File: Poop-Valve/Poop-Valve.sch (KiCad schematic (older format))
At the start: 45 parts, among them J1 RaspberryPi, J10 Valve Sig, J11 Conn_01x02_Male, J12 Relays, J13 LEDs, J14 24VDC, J15 Sensor, J16 Grove LCD, J2 Valve, J3 Charger, J4 Override, J5 Ovr Switch, J6 Power, J7 12VDC, J8 Conn_01x02_Male, J9 Conn_01x02_Male, K1 Override Relays, K2 Polarity Reverse, K3 Enable Relays, K4 Relay_Module, K5 Direction Relays, K6 Polarity Reverse, SW1 Override, SW2 SW_DPDT_x2, SW3 Open/Close, U1 Opened, U2 Closed, U3 Override, U4 MCP3008

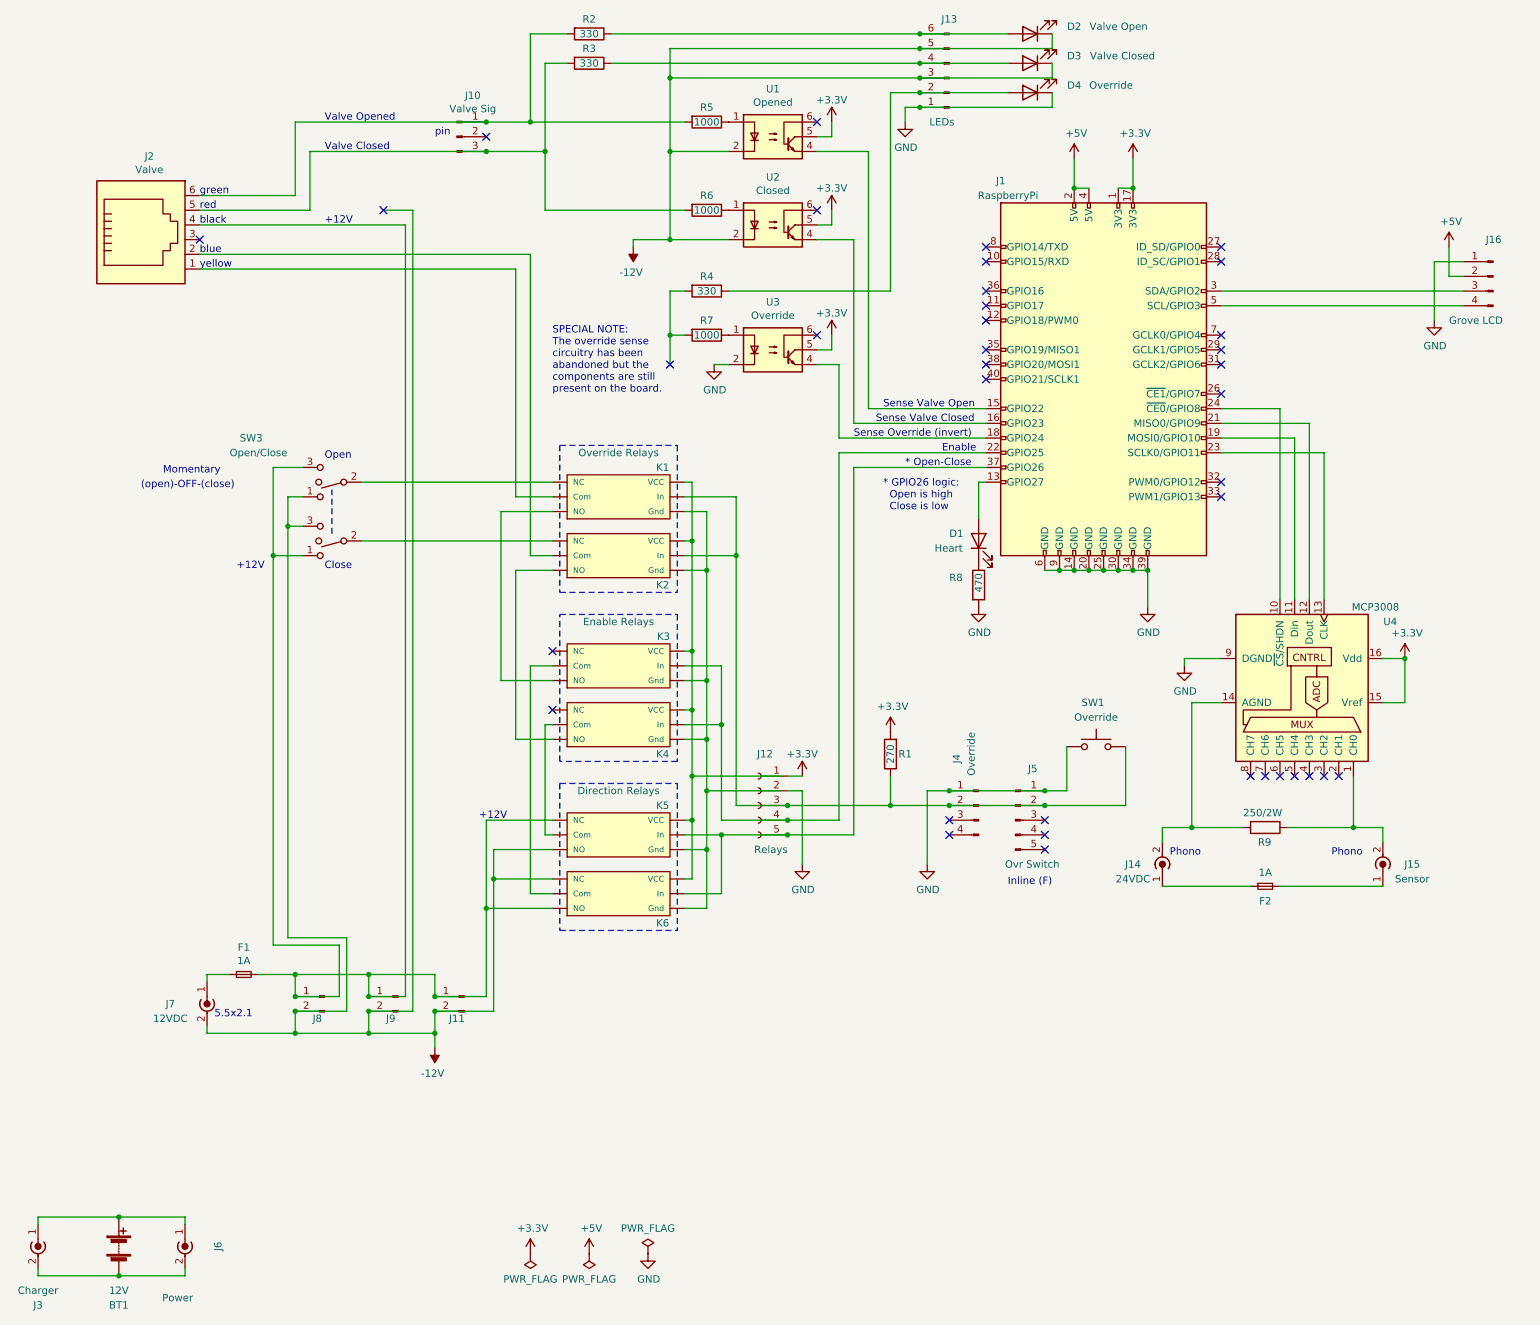
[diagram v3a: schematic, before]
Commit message: v0.9 add override shunt and sense transistors
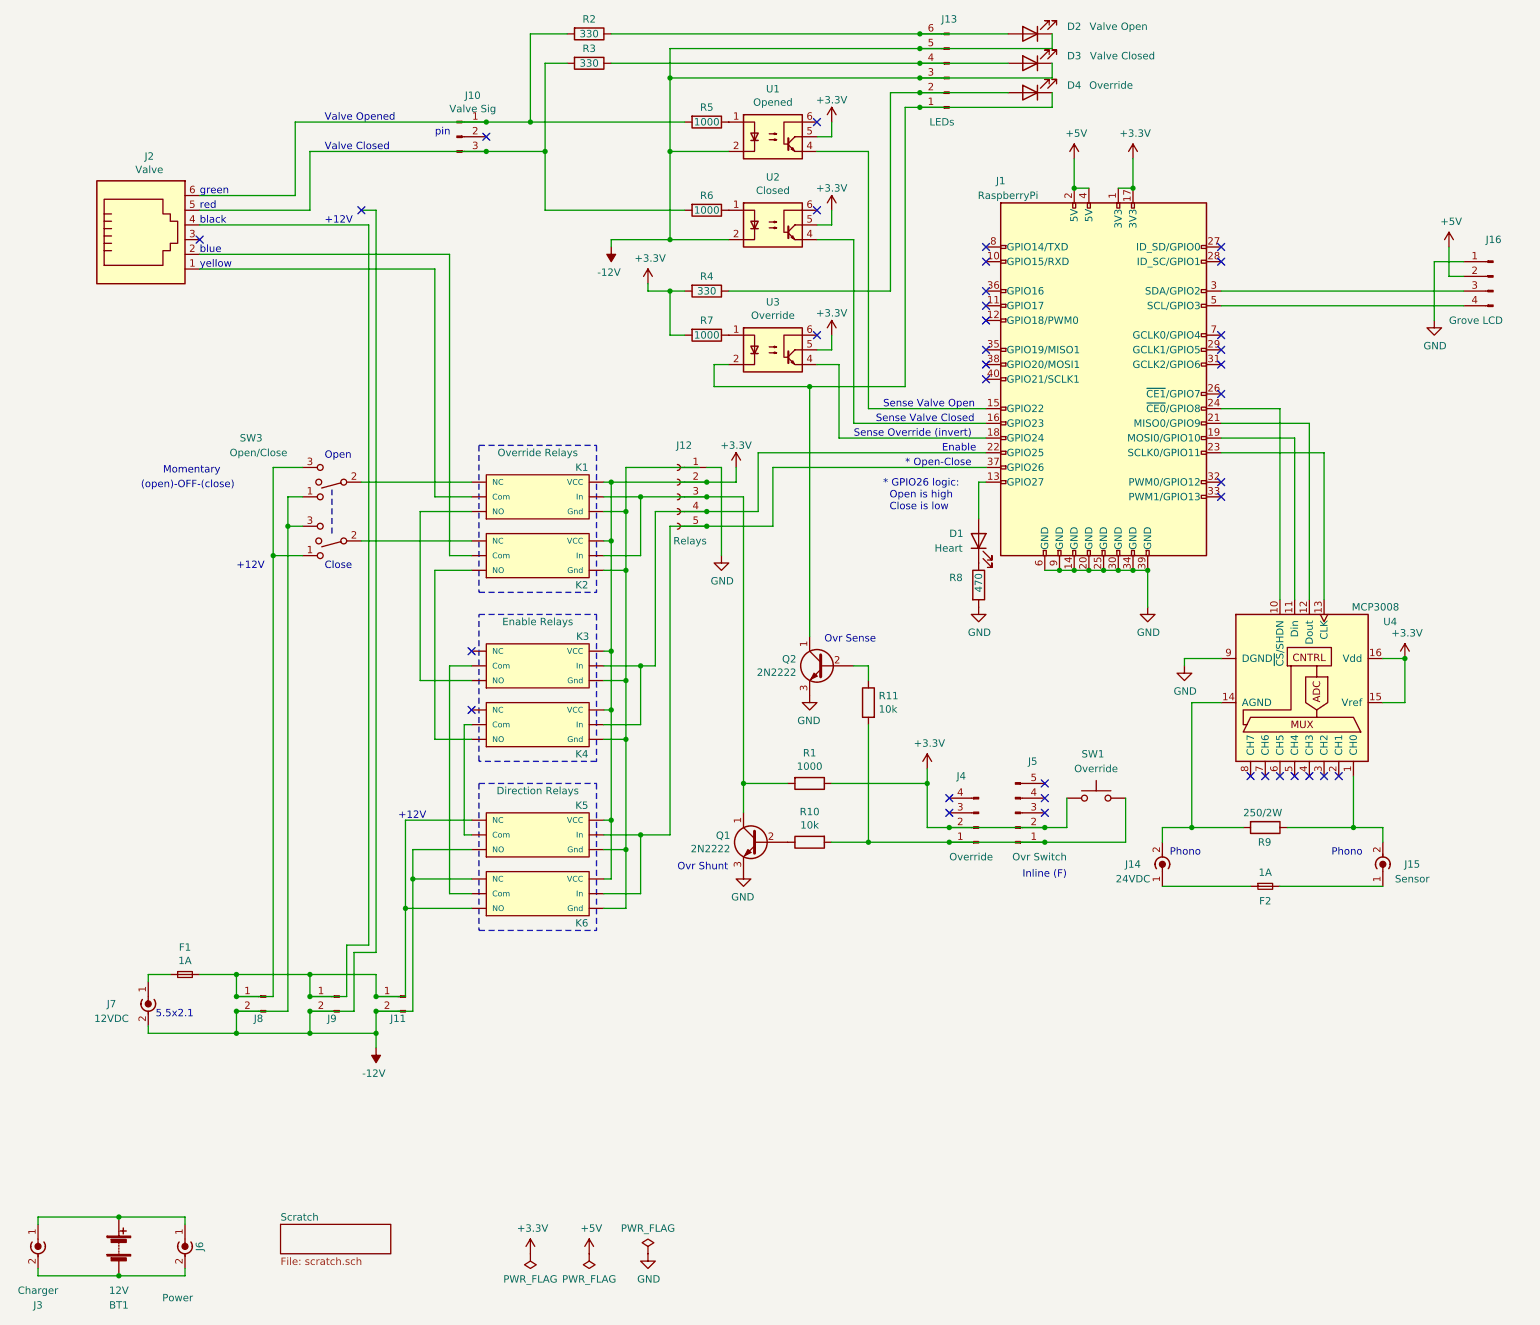
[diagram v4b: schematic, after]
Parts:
- added Q1, Q2: 2N2222, symbol Device:Q_NPN_CBE
- added R10, R11: 10k, symbol Device:R
- R1: value 270 -> 1000
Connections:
- net +3V3: now also J12.2 (Pin_2), J4.2 (Pin_2), J5.2 (Pin_2), K1.~ (VCC), K2.~ (VCC), K3.~ (VCC), K4.~ (VCC), K5.~ (VCC), K6.~ (VCC), R1.1, R4.2, R7.2, SW1.2; no longer J12.1 (Pin_1), R1.2
- net GND: now also J12.1 (Pin_1), Q1.3 (E), Q2.3 (E); no longer D4.1 (K), J12.2 (Pin_2), J13.1 (Pin_1), J4.1 (Pin_1), J5.1 (Pin_1), SW1.2, U3.2
- new net: K1.~ (VCC), K2.~ (VCC), K3.~ (VCC), K4.~ (VCC), K5.~ (VCC), K6.~ (VCC)
- new net: K1.~ (VCC), K3.~ (VCC)
- new net: K3.~ (VCC), K6.~ (VCC)
- new net: K2.~ (VCC), K4.~ (VCC)
- new net: K4.~ (VCC), K5.~ (VCC)
- new net: D4.1 (K), J13.1 (Pin_1), Q2.1 (C), U3.2
- new net: J4.1 (Pin_1), J5.1 (Pin_1), R10.2, R11.2, SW1.1
- new net: J12.3 (Pin_3), K1.~ (VCC), K2.~ (VCC), Q1.1 (C), R1.2
- new net: Q1.2 (B), R10.1
- new net: Q2.2 (B), R11.1
- no-connect marks 37 -> 36
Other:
- note added: "Ovr Sense"
- note added: "Ovr Shunt"
- note removed: "SPECIAL NOTE:\nThe override sense\ncircuitry has been\nabandoned but the\ncomponents are still\npresent on the board."
- moved on the sheet: F1, J11, J12, J4, J5, J7, J8, J9, K1, K2, K3, K4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

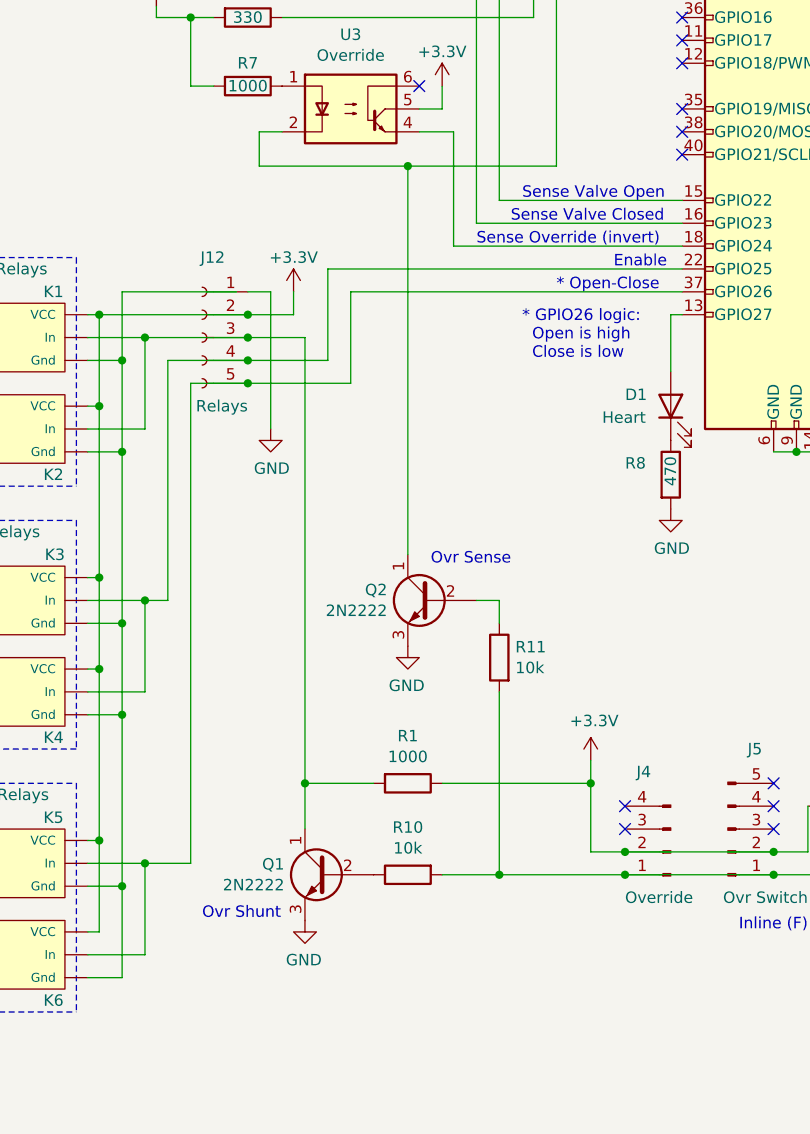
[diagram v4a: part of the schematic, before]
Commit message: v0.10 add Master Override switch
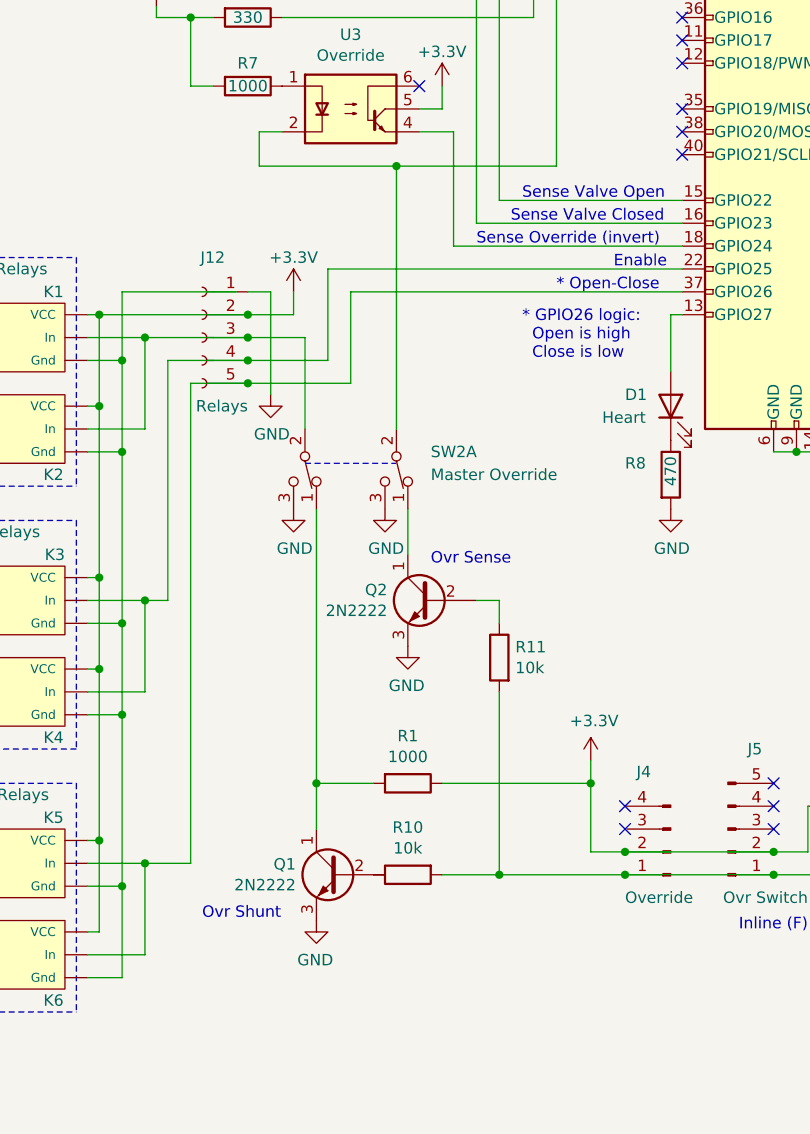
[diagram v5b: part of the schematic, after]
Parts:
- added SW2: Master Override, symbol Switch:SW_SPDT_SMALL
- added SW?: SW_SPDT_SMALL, symbol Switch:SW_SPDT_SMALL
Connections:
- net GND: now also SW2.3 (C), SW?.3 (C)
- net at D4.1 (K), J13.1 (Pin_1), U3.2: now also SW2.2 (B); no longer Q2.1 (C)
- net at Q1.2 (B): no longer R10.1
- new net: K1.~ (VCC), K2.~ (VCC), K3.~ (VCC), K4.~ (VCC), K5.~ (VCC), K6.~ (VCC)
- new net: K1.~ (VCC), K3.~ (VCC)
- new net: K3.~ (VCC), K6.~ (VCC)
- new net: K2.~ (VCC), K4.~ (VCC)
- new net: K4.~ (VCC), K5.~ (VCC)
- new net: J12.3 (Pin_3), K1.~ (VCC), K2.~ (VCC), SW?.2 (B)
- new net: Q1.1 (C), R1.2, SW?.1 (A)
- new net: Q2.1 (C), SW2.1 (A)
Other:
- moved on the sheet: Q1
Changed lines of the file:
@@
 Sheet 1 2
 Title "Poop Valve Controller"
-Date "2023-01-29"
-Rev "0.9 (draft)"
+Date "2023-02-01"
+Rev "0.10 (draft)"
 Comp "Robert Ferguson Observatory"
-Comment1 "v0.6 fix led connector pinout"
-Comment2 "v0.7 correct ADC sample wiring"
-Comment3 "v0.8 reconfigure manual override; updated layout for clarity"
-Comment4 "v0.9 add override shunt and sense transistors "
+Comment1 "v0.7 correct ADC sample wiring"
+Comment2 "v0.8 reconfigure manual override; updated layout for clarity"
+Comment3 "v0.9 add override shunt and sense transistors "
+Comment4 "v0.10 add Master Override switch"
 $EndDescr
 $Comp
@@
 Wire Wire Line
 	4700 2500 4800 2500
-$Comp
-L power:GND #PWR012
-U 1 1 65D19661
-P 5050 4300
-F 0 "#PWR012" H 5050 4050 50  0001 C CNN
-F 1 "GND" H 5055 4127 50  0000 C CNN
-F 2 "" H 5050 4300 50  0001 C CNN
-F 3 "" H 5050 4300 50  0001 C CNN
-	1    5050 4300
-	1    0    0    -1
-$EndComp
 Wire Wire Line
 	4950 3900 5200 3900
@@
 L Device:Q_NPN_CBE Q?
 U 1 1 6627A4F5
-P 5300 6250
+P 5350 6250
 AR Path="/65DFE627/6627A4F5" Ref="Q?"  Part="1"
 AR Path="/6627A4F5" Ref="Q1"  Part="1"
-F 0 "Q1" H 5490 6296 50  0000 L CNN
-F 1 "2N2222" H 5490 6205 50  0000 L CNN
-F 2 "" H 5500 6350 50  0001 C CNN
-F 3 "~" H 5300 6250 50  0001 C CNN
-	1    5300 6250
+F 0 "Q1" H 5540 6296 50  0000 L CNN
+F 1 "2N2222" H 5540 6205 50  0000 L CNN
+F 2 "" H 5550 6350 50  0001 C CNN
+F 3 "~" H 5350 6250 50  0001 C CNN
+	1    5350 6250
 	-1   0    0    -1
 $EndComp
@@
 L power:GND #PWR?
 U 1 1 6627A53E
-P 5200 6450
+P 5250 6450
 AR Path="/65DFE627/6627A53E" Ref="#PWR?"  Part="1"
 AR Path="/6627A53E" Ref="#PWR021"  Part="1"
-F 0 "#PWR021" H 5200 6200 50  0001 C CNN
-F 1 "GND" H 5205 6277 50  0000 C CNN
-F 2 "" H 5200 6450 50  0001 C CNN
-F 3 "" H 5200 6450 50  0001 C CNN
-	1    5200 6450
+F 0 "#PWR021" H 5250 6200 50  0001 C CNN
+F 1 "GND" H 5255 6277 50  0000 C CNN
+F 2 "" H 5250 6450 50  0001 C CNN
+F 3 "" H 5250 6450 50  0001 C CNN
+	1    5250 6450
 	-1   0    0    -1
 $EndComp
@@
 Text Notes 4750 6450 0    50   ~ 0
 Ovr Shunt
-Wire Wire Line
-	5200 3900 5200 5850
-Wire Wire Line
-	5500 5850 5200 5850
-Connection ~ 5200 5850
-Wire Wire Line
-	5200 5850 5200 6050
+Connection ~ 5250 5850
+Wire Wire Line
+	5250 5850 5250 6050
 Connection ~ 6450 5850
 Wire Wire Line
@@
 Wire Wire Line
 	5800 5850 6450 5850
+$Comp
+L Device:R R?
+U 1 1 6659FCFC
+P 6050 5300
+AR Path="/65DFE627/6659FCFC" Ref="R?"  Part="1"
+AR Path="/6659FCFC" Ref="R11"  Part="1"
+F 0 "R11" H 5980 5346 50  0000 R CNN
+F 1 "10k" H 5980 5255 50  0000 R CNN
+F 2 "" V 5980 5300 50  0001 C CNN
+F 3 "~" H 6050 5300 50  0001 C CNN
+	1    6050 5300
+	-1   0    0    -1
+$EndComp
+$Comp
+L power:GND #PWR?
+U 1 1 6659FD02
+P 5650 5250
+AR Path="/65DFE627/6659FD02" Ref="#PWR?"  Part="1"
+AR Path="/6659FD02" Ref="#PWR022"  Part="1"
+F 0 "#PWR022" H 5650 5000 50  0001 C CNN
+F 1 "GND" H 5655 5077 50  0000 C CNN
+F 2 "" H 5650 5250 50  0001 C CNN
+F 3 "" H 5650 5250 50  0001 C CNN
+	1    5650 5250
+	-1   0    0    -1
+$EndComp
+Wire Wire Line
+	5000 3000 5000 3150
+$Comp
+L power:+3.3V #PWR011
+U 1 1 6660F16D
+P 4550 2450
+F 0 "#PWR011" H 4550 2300 50  0001 C CNN
+F 1 "+3.3V" H 4565 2623 50  0000 C CNN
+F 2 "" H 4550 2450 50  0001 C CNN
+F 3 "" H 4550 2450 50  0001 C CNN
+	1    4550 2450
+	1    0    0    -1
+$EndComp
+Connection ~ 4700 2500
+Wire Wire Line
+	4300 2150 4300 2200
+Wire Wire Line
+	4300 2150 4700 2150
+Wire Wire Line
+	4550 2450 4550 2500
+Wire Wire Line
+	4550 2500 4700 2500
+Wire Wire Line
+	6300 1250 6300 3150
+Connection ~ 6050 6250
+Wire Wire Line
+	6050 6250 6600 6250
+Wire Wire Line
+	5950 5050 6050 5050
+Wire Wire Line
+	6050 5450 6050 6250
+Wire Wire Line
+	6050 5050 6050 5150
+Wire Wire Line
+	7800 5950 7800 6250
+Wire Wire Line
+	7400 5950 7400 6150
+Wire Wire Line
+	7250 6250 7800 6250
+$Comp
+L Switch:SW_Push SW1
+U 1 1 63F2028E
+P 7600 5950
+F 0 "SW1" H 7700 6250 50  0000 R CNN
+F 1 "Override" H 7750 6150 50  0000 R CNN
+F 2 "" H 7600 6150 50  0001 C CNN
+F 3 "~" H 7600 6150 50  0001 C CNN
+	1    7600 5950
+	-1   0    0    -1
+$EndComp
+Wire Wire Line
+	5150 3800 5150 3700
+Wire Wire Line
+	5050 3700 5050 4150
+Wire Wire Line
+	4300 3800 4950 3800
+Connection ~ 4300 3800
+Connection ~ 4950 3800
+Wire Wire Line
+	4950 3800 5150 3800
+Wire Wire Line
+	4400 3700 4400 4000
+Connection ~ 4400 4000
+Text Notes 5750 4900 0    50   ~ 0
+Ovr Sense
 $Comp
 L Device:Q_NPN_CBE Q?
@@
 	-1   0    0    -1
 $EndComp
-$Comp
-L Device:R R?
-U 1 1 6659FCFC
-P 6050 5300
-AR Path="/65DFE627/6659FCFC" Ref="R?"  Part="1"
-AR Path="/6659FCFC" Ref="R11"  Part="1"
-F 0 "R11" H 5980 5346 50  0000 R CNN
-F 1 "10k" H 5980 5255 50  0000 R CNN
-F 2 "" V 5980 5300 50  0001 C CNN
-F 3 "~" H 6050 5300 50  0001 C CNN
-	1    6050 5300
-	-1   0    0    -1
-$EndComp
+Wire Wire Line
+	5650 4650 5650 4850
+$Comp
+L Switch:SW_SPDT_SMALL SW?
+U 1 1 66A95683
+P 5200 4500
+F 0 "SW?" V 5129 4598 50  0001 L CNN
+F 1 "SW_SPDT_SMALL" V 5550 4100 50  0001 L CNN
+F 2 "" H 5150 4270 50  0001 C CNN
+F 3 "~" H 5150 4270 50  0001 C CNN
+	1    5200 4500
+	0    1    1    0
+$EndComp
+Wire Wire Line
+	5250 4650 5250 5850
+Wire Wire Line
+	5500 5850 5250 5850
+Wire Wire Line
+	5200 4300 5200 3900
+Wire Wire Line
+	5600 4300 5600 3150
+Connection ~ 5600 3150
+Wire Wire Line
+	5600 3150 5000 3150
+Wire Wire Line
+	5600 3150 6300 3150
 $Comp
 L power:GND #PWR?
-U 1 1 6659FD02
-P 5650 5250
-AR Path="/65DFE627/6659FD02" Ref="#PWR?"  Part="1"
-AR Path="/6659FD02" Ref="#PWR022"  Part="1"
-F 0 "#PWR022" H 5650 5000 50  0001 C CNN
-F 1 "GND" H 5655 5077 50  0000 C CNN
-F 2 "" H 5650 5250 50  0001 C CNN
-F 3 "" H 5650 5250 50  0001 C CNN
-	1    5650 5250
-	-1   0    0    -1
-$EndComp
-Text Notes 5750 4900 0    50   ~ 0
-Ovr Sense
-Wire Wire Line
-	5000 3000 5000 3150
-$Comp
-L power:+3.3V #PWR011
-U 1 1 6660F16D
-P 4550 2450
-F 0 "#PWR011" H 4550 2300 50  0001 C CNN
-F 1 "+3.3V" H 4565 2623 50  0000 C CNN
-F 2 "" H 4550 2450 50  0001 C CNN
-F 3 "" H 4550 2450 50  0001 C CNN
-	1    4550 2450
-	1    0    0    -1
-$EndComp
-Connection ~ 4700 2500
-Wire Wire Line
-	4300 2150 4300 2200
-Wire Wire Line
-	4300 2150 4700 2150
-Wire Wire Line
-	4550 2450 4550 2500
-Wire Wire Line
-	4550 2500 4700 2500
-Wire Wire Line
-	6300 3150 5650 3150
-Wire Wire Line
-	6300 1250 6300 3150
-Connection ~ 5650 3150
-Wire Wire Line
-	5650 3150 5000 3150
-Wire Wire Line
-	5650 3150 5650 4850
-Connection ~ 6050 6250
-Wire Wire Line
-	6050 6250 6600 6250
-Wire Wire Line
-	5950 5050 6050 5050
-Wire Wire Line
-	6050 5450 6050 6250
-Wire Wire Line
-	6050 5050 6050 5150
-Wire Wire Line
-	7800 5950 7800 6250
-Wire Wire Line
-	7400 5950 7400 6150
-Wire Wire Line
-	7250 6250 7800 6250
-$Comp
-L Switch:SW_Push SW1
-U 1 1 63F2028E
-P 7600 5950
-F 0 "SW1" H 7700 6250 50  0000 R CNN
-F 1 "Override" H 7750 6150 50  0000 R CNN
-F 2 "" H 7600 6150 50  0001 C CNN
-F 3 "~" H 7600 6150 50  0001 C CNN
-	1    7600 5950
-	-1   0    0    -1
-$EndComp
-Wire Wire Line
-	5150 3800 5150 3700
-Wire Wire Line
-	5050 3700 5050 4300
-Wire Wire Line
-	4300 3800 4950 3800
-Connection ~ 4300 3800
-Connection ~ 4950 3800
-Wire Wire Line
-	4950 3800 5150 3800
-Wire Wire Line
-	4400 3700 4400 4000
-Connection ~ 4400 4000
+U 1 1 66BEBFAF
+P 5550 4650
+F 0 "#PWR?" H 5550 4400 50  0001 C CNN
+F 1 "GND" H 5555 4477 50  0000 C CNN
+F 2 "" H 5550 4650 50  0001 C CNN
+F 3 "" H 5550 4650 50  0001 C CNN
+	1    5550 4650
+	1    0    0    -1
+$EndComp
+$Comp
+L power:GND #PWR?
+U 1 1 66BECFD3
+P 5150 4650
+F 0 "#PWR?" H 5150 4400 50  0001 C CNN
+F 1 "GND" H 5155 4477 50  0000 C CNN
+F 2 "" H 5150 4650 50  0001 C CNN
+F 3 "" H 5150 4650 50  0001 C CNN
+	1    5150 4650
+	1    0    0    -1
+$EndComp
+$Comp
+L power:GND #PWR012
+U 1 1 65D19661
+P 5050 4150
+F 0 "#PWR012" H 5050 3900 50  0001 C CNN
+F 1 "GND" H 5055 3977 50  0000 C CNN
+F 2 "" H 5050 4150 50  0001 C CNN
+F 3 "" H 5050 4150 50  0001 C CNN
+	1    5050 4150
+	1    0    0    -1
+$EndComp
+Wire Notes Line
+	5200 4450 5600 4450
+$Comp
+L Switch:SW_SPDT_SMALL SW2
+U 1 1 66A5A149
+P 5600 4500
+F 0 "SW2" V 5500 4650 50  0000 L CNN
+F 1 "Master Override" V 5600 4650 50  0000 L CNN
+F 2 "" H 5550 4270 50  0001 C CNN
+F 3 "~" H 5550 4270 50  0001 C CNN
+	1    5600 4500
+	0    1    1    0
+$EndComp
 $EndSCHEMATC
